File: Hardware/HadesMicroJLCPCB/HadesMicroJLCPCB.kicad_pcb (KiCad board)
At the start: 4 copper layers, 50 x 50 mm, 88 parts, among them IC1 MPRLS0015PA0000SA, U1 AP2112K-3.3, U2 PCA9685PW, U3 CAT24C256, U4 USBLC6-2SC6, U5 74AHC1GU04GW,125, U6 CH340E

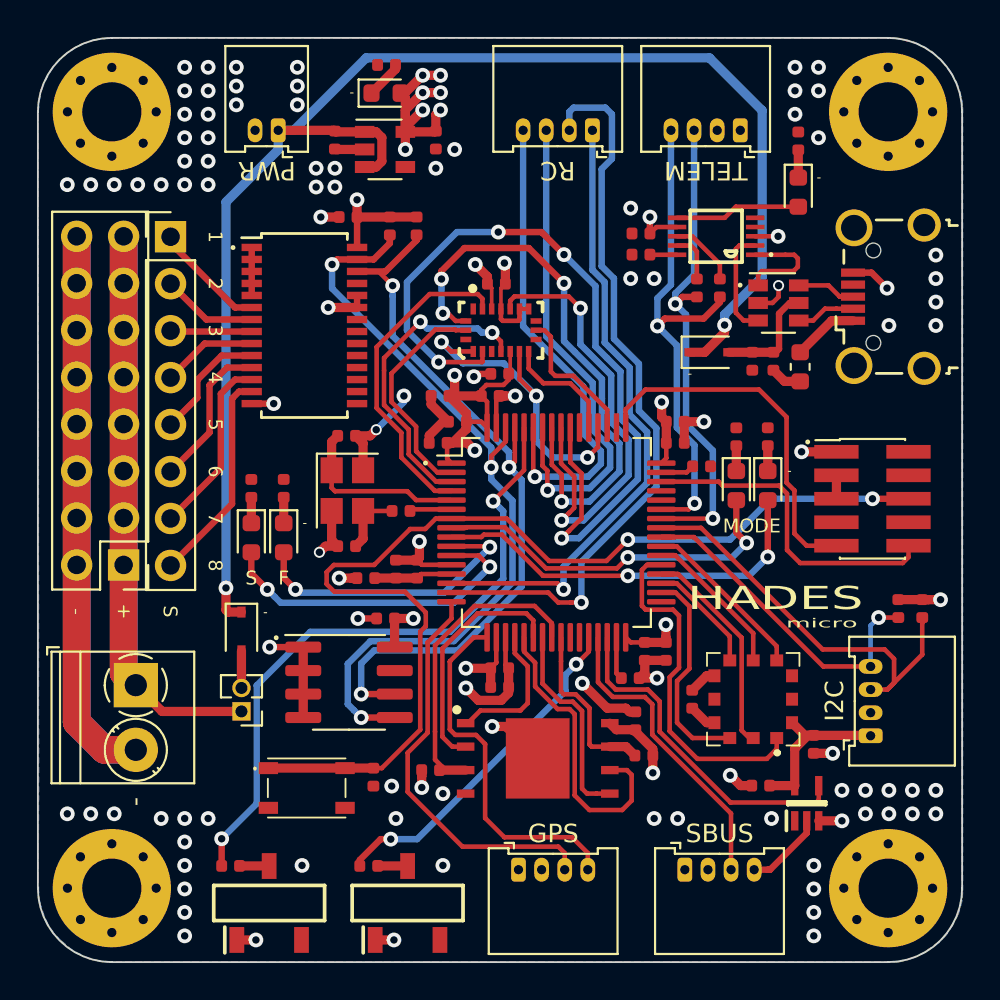
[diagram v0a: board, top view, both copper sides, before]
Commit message: Updated Hades Micro (JLCPCB) silkscreen.
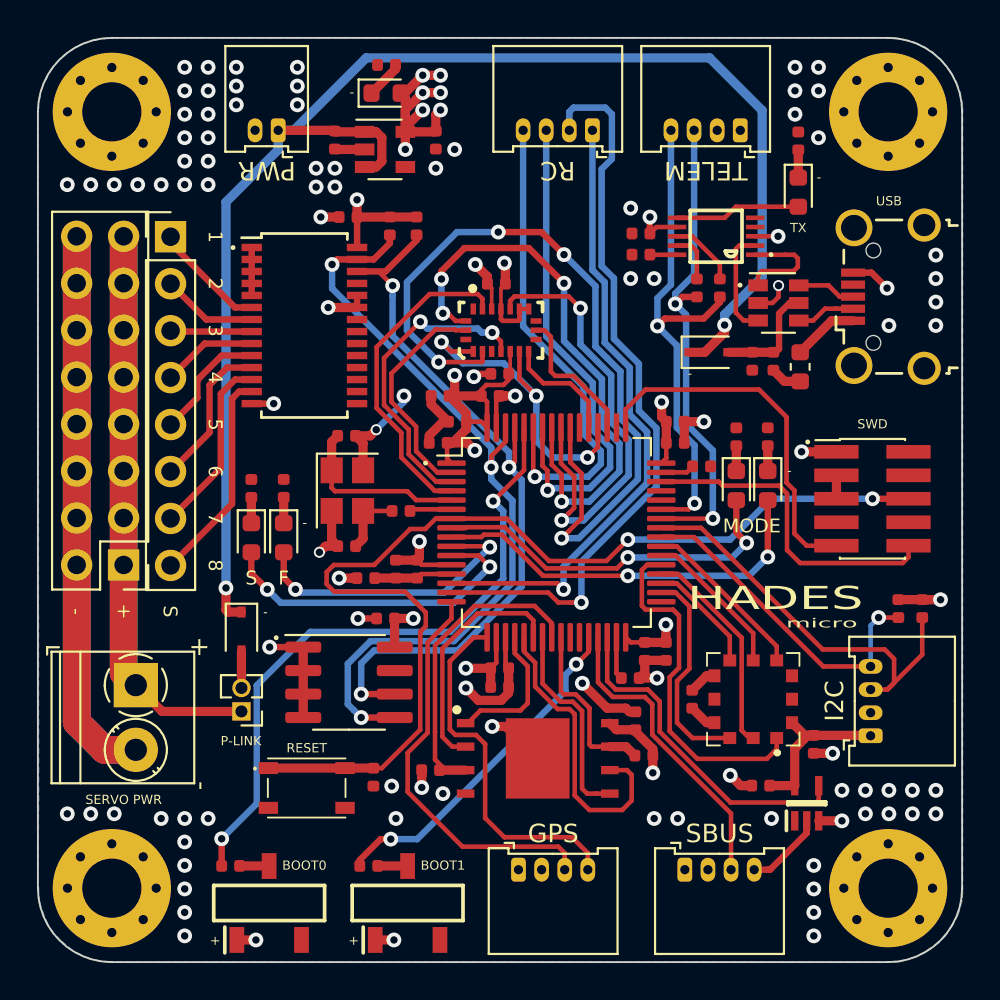
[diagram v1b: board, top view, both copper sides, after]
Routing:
- net GND: vias 98 -> 96
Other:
- board text added: "BOOT0"
- board text added: "BOOT1"
- board text added: "P-LINK"
- board text added: "RESET"
- board text added: "SERVO PWR"
- board text added: "SWD"
- board text added: "USB"
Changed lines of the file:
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@@
   (general
     (thickness 1.6)
-    (drawings 113)
-    (tracks 1077)
+    (drawings 124)
+    (tracks 1075)
     (zones 0)
     (modules 88)
@@
     )
   )
+  (gr_text TX (at 61.1378 30.2768) (layer F.SilkS)
+    (effects (font (size 0.5 0.5) (thickness 0.1)))
+  )
+  (gr_text + (at 28.702 52.959 90) (layer F.SilkS)
+    (effects (font (size 1 1) (thickness 0.1)))
+  )
+  (gr_text USB (at 66.04 28.829) (layer F.SilkS)
+    (effects (font (size 0.5 0.5) (thickness 0.1)))
+  )
+  (gr_text "SERVO PWR" (at 24.638 61.214) (layer F.SilkS)
+    (effects (font (size 0.5 0.5) (thickness 0.1)))
+  )
+  (gr_text P-LINK (at 30.988 58.039) (layer F.SilkS)
+    (effects (font (size 0.5 0.5) (thickness 0.1)))
+  )
+  (gr_text SWD (at 65.151 40.894) (layer F.SilkS)
+    (effects (font (size 0.5 0.5) (thickness 0.1)))
+  )
+  (gr_text RESET (at 34.544 58.42) (layer F.SilkS)
+    (effects (font (size 0.5 0.5) (thickness 0.1)))
+  )
+  (gr_text + (at 37.084 68.834) (layer F.SilkS)
+    (effects (font (size 0.5 0.5) (thickness 0.1)))
+  )
+  (gr_text + (at 29.591 68.834) (layer F.SilkS)
+    (effects (font (size 0.5 0.5) (thickness 0.1)))
+  )
+  (gr_text BOOT1 (at 41.91 64.77) (layer F.SilkS)
+    (effects (font (size 0.5 0.5) (thickness 0.1)))
+  )
+  (gr_text BOOT0 (at 34.417 64.77) (layer F.SilkS)
+    (effects (font (size 0.5 0.5) (thickness 0.1)))
+  )
   (gr_text GND (at 31.7754 22.9362 90) (layer B.SilkS)
     (effects (font (size 0.75 0.75) (thickness 0.1)) (justify mirror))
@@
     (effects (font (size 0.75 0.75) (thickness 0.1)))
   )
-  (gr_text - (at 25.2476 61.3156 90) (layer F.SilkS)
+  (gr_text - (at 28.702 60.452 90) (layer F.SilkS)
     (effects (font (size 1 1) (thickness 0.1)))
   )
@@
   (via (at 21.59 61.976) (size 0.8) (drill 0.4) (layers F.Cu B.Cu) (net 2))
   (via (at 22.86 61.976) (size 0.8) (drill 0.4) (layers F.Cu B.Cu) (net 2))
-  (via (at 34.29 64.77) (size 0.8) (drill 0.4) (layers F.Cu B.Cu) (net 2))
-  (via (at 41.91 64.77) (size 0.8) (drill 0.4) (layers F.Cu B.Cu) (net 2))
   (via (at 53.34 62.23) (size 0.8) (drill 0.4) (layers F.Cu B.Cu) (net 2))
   (via (at 54.61 62.23) (size 0.8) (drill 0.4) (layers F.Cu B.Cu) (net 2))

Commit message: NAVC debug software real-time plotting.
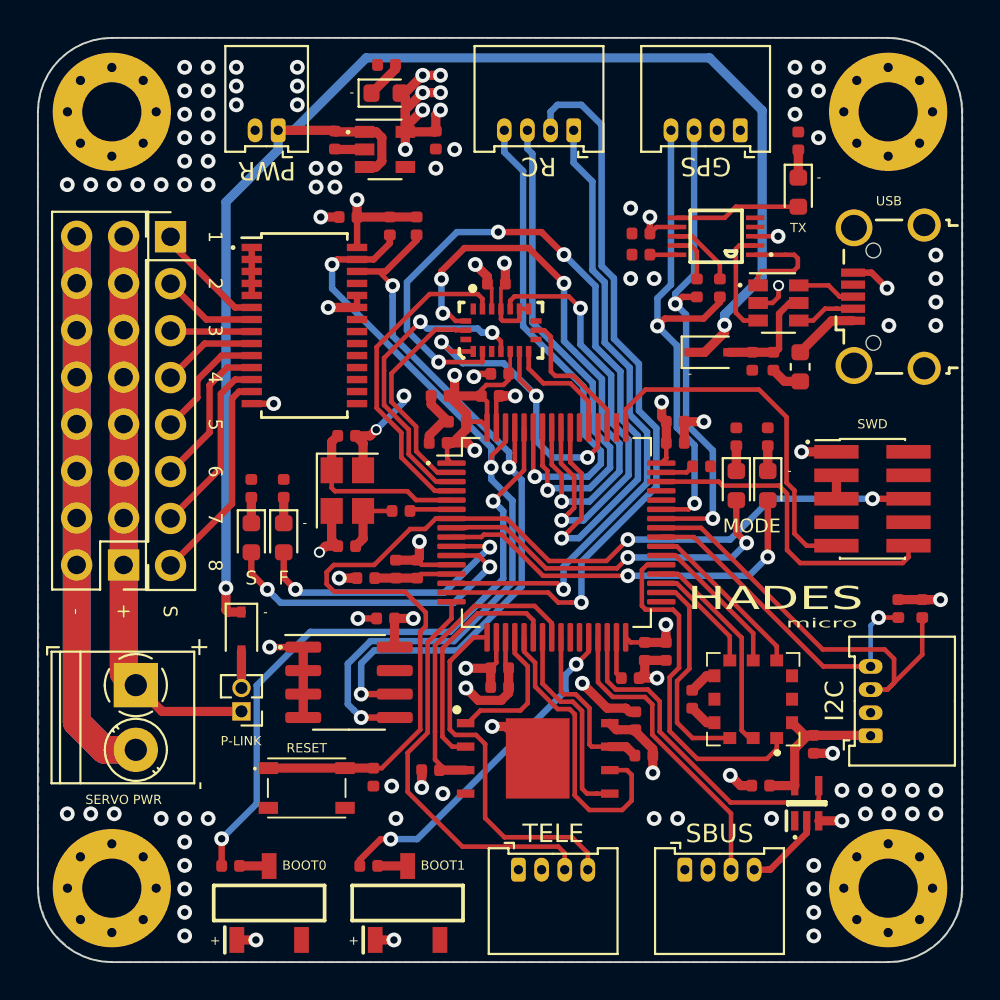
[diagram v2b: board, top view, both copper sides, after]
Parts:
- moved RC 1.02 mm to (49.0, 25.0)
- renumbered TELEM to TELE
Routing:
- net GND: vias 96 -> 95
- net (no net): vias 0 -> 1
